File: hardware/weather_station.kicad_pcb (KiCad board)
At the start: 2 copper layers, 70 parts, among them J1 USB_MICRO, Q1 BD135, Q2 BD135, SW1 SWITCH_SPDT, U1 nRF51x22, U2 TMP112, U3 BMP280, U4 Si7013, U5 LM3668, U6 MCP73831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

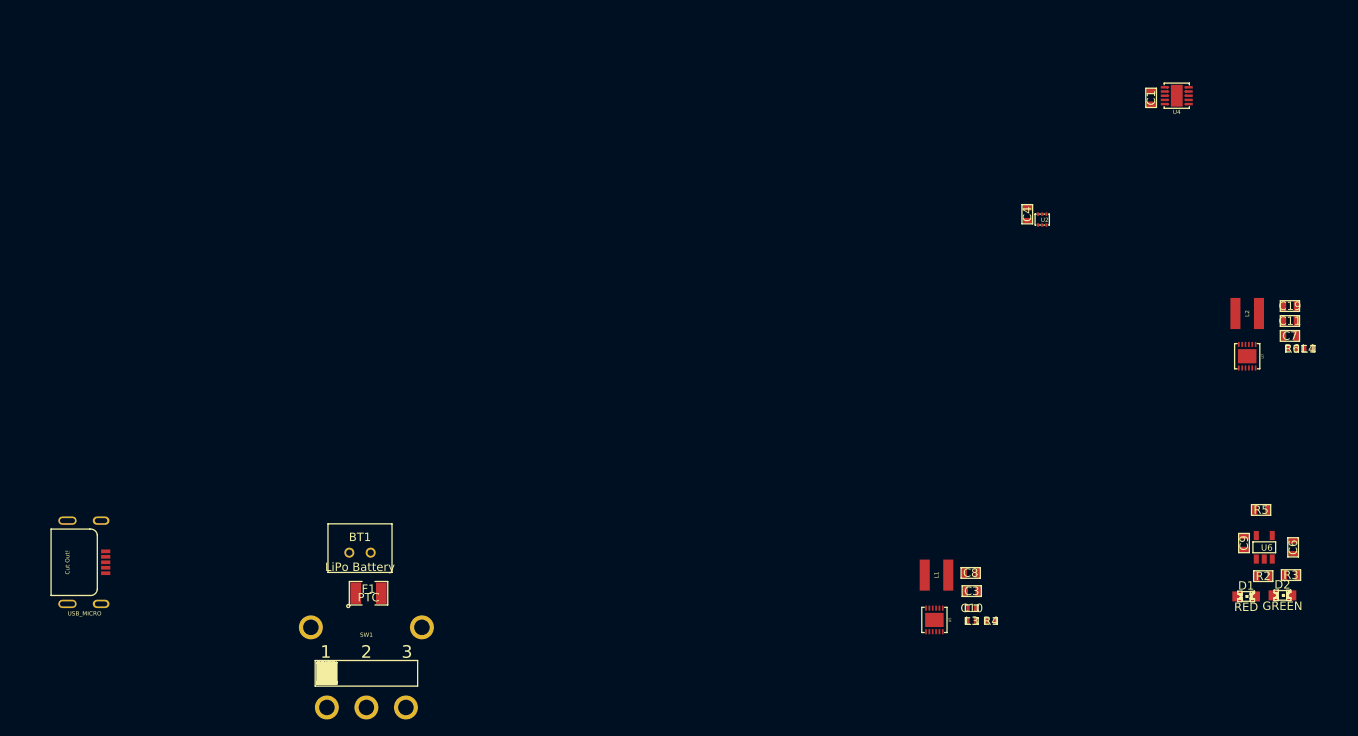
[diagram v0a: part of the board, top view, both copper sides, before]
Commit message: Update layout. Place some groups of components strategically
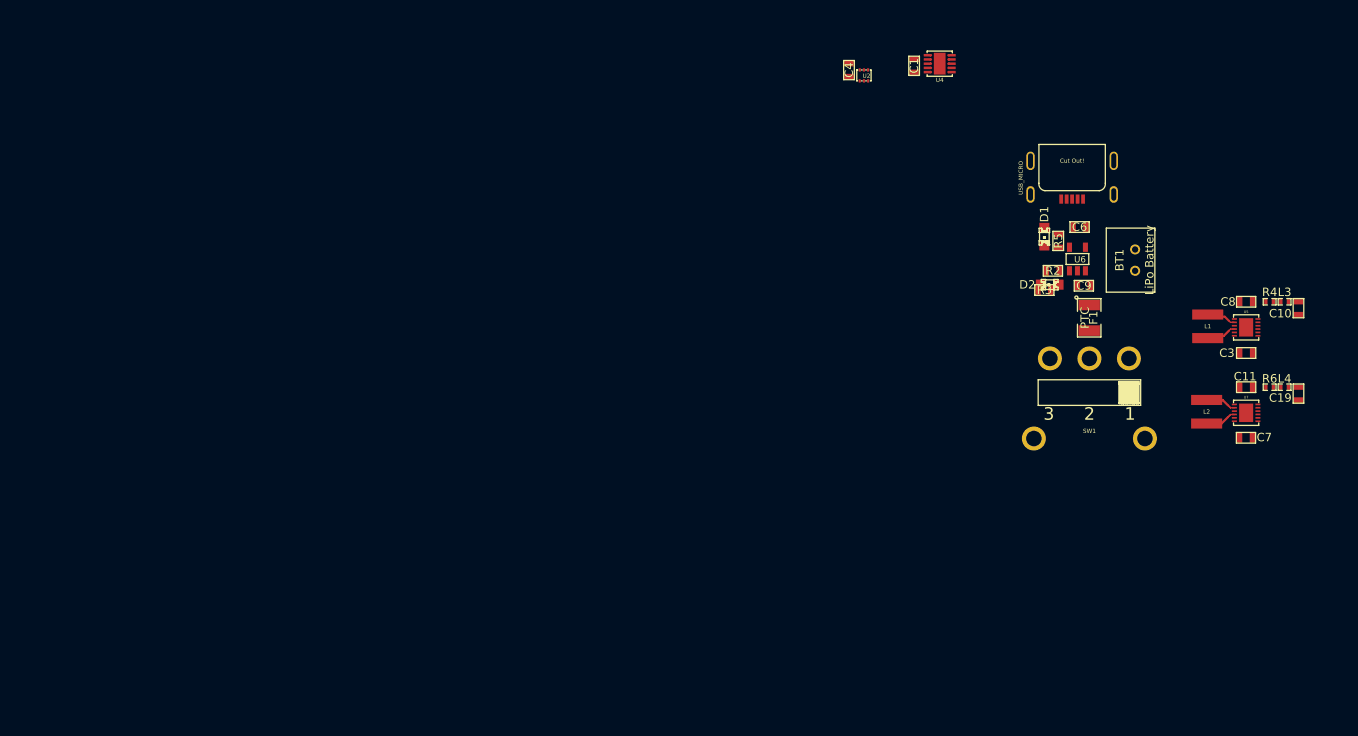
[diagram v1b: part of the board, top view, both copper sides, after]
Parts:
- C10: footprint SMD_Packages:SMD-0402 -> SMD_Packages:SMD-0603
- moved J1 128.7 mm to (234.4, 98.3), turned to 180 degrees
- moved BT1 98.6 mm to (241.9, 110.1), turned to 90 degrees
- moved SW1 95.5 mm to (236.5, 121.8), turned to 180 degrees
- moved F1 91.8 mm to (236.5, 117.0), turned to 270 degrees
- moved L3 53.2 mm to (259.7, 115.1)
- moved C10 52.8 mm to (261.4, 115.8), turned to 270 degrees
- moved U5 50.9 mm to (255.1, 118.1), turned to 90 degrees
- moved R4 50.4 mm to (257.9, 115.1), turned to 180 degrees
- moved D1 49.1 mm to (231.1, 107.3), turned to 270 degrees
- moved D2 46.2 mm to (231.8, 113.0), turned to 180 degrees
- moved C8 46.0 mm to (255.1, 115.1), turned to 180 degrees
- moved C6 45.8 mm to (235.3, 106.2), turned to 180 degrees
- moved R3 44.8 mm to (231.1, 113.7), turned to 180 degrees
- moved R2 44.1 mm to (232.2, 111.4)
- moved L1 43.8 mm to (250.6, 118.0), turned to 270 degrees
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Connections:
- U5 pad 11: GND -> Net-(C8-Pad1)
- U5 pad 12: VIN -> Net-(C8-Pad1)
- U5 pad 7: Net-(C8-Pad1) -> VIN
- U5 pad 8: Net-(C8-Pad1) -> GND
- U7 pad 11: GND -> Net-(C11-Pad1)
- U7 pad 12: VIN -> Net-(C11-Pad1)
- U7 pad 7: Net-(C11-Pad1) -> VIN
- U7 pad 8: Net-(C11-Pad1) -> GND
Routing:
- net Net-(L2-Pad1): track 0.00 -> 7.30 mm
- net Net-(L2-Pad2): track 0.00 -> 5.26 mm
- net Net-(L1-Pad2): track 0.00 -> 3.62 mm
- net Net-(L1-Pad1): track 0.00 -> 3.56 mm
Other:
- net class Default: clearance 0.254 -> 0.1524
- net class Default2 added: clearance 0.1524, trace_width 0.254, via_dia 0.889, via_drill 0.635
- net class Default3 added: clearance 0.254, trace_width 0.254, via_dia 0.889, via_drill 0.635
- rule trace_clearance: 0.254 -> 0.1524
- rule trace_min: 0.254 -> 0.1524
- rule via_min_drill: 0.508 -> 0.1778
- rule via_min_size: 0.889 -> 0.3302

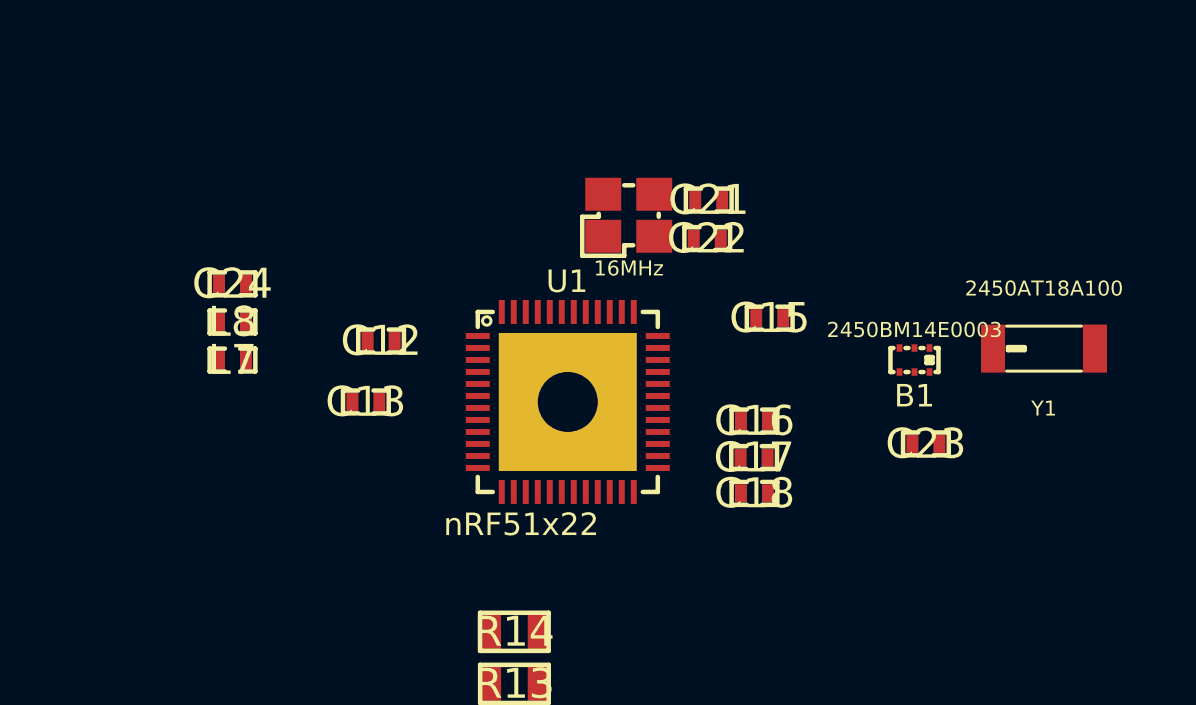
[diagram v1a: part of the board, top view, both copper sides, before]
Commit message: Place components around nRF51 device
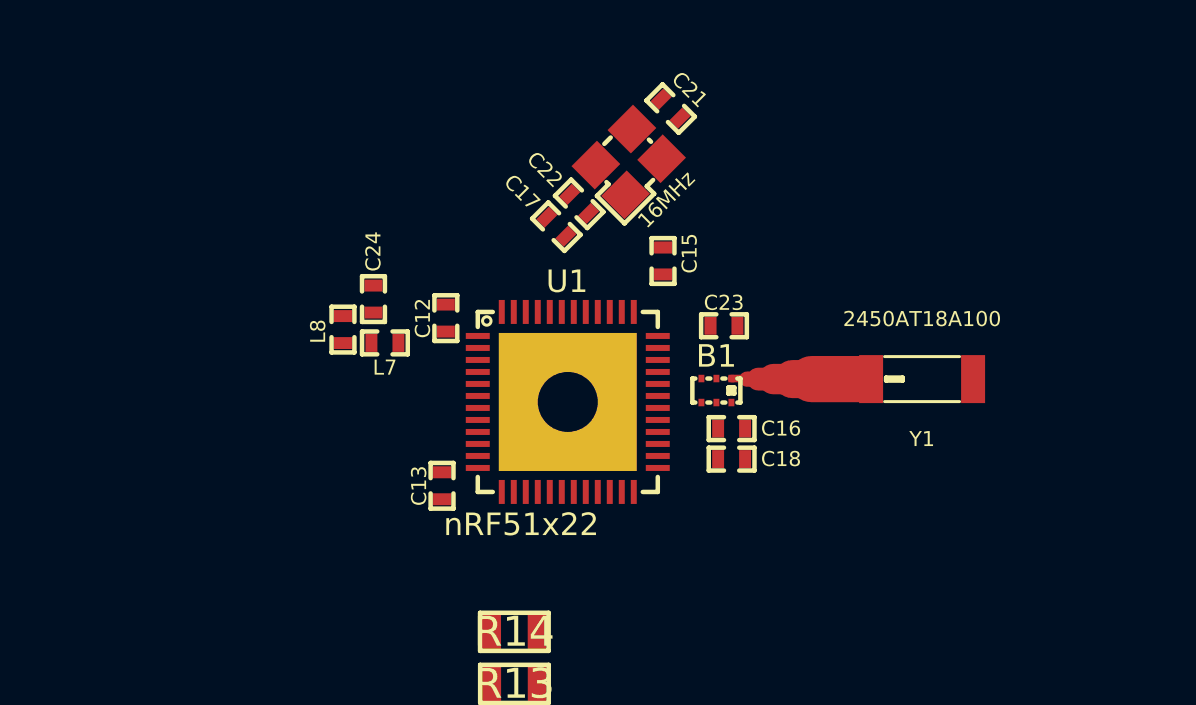
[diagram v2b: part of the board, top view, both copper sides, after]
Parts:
- moved C17 10.1 mm to (247.1, 35.7), turned to 135 degrees
- moved C23 7.80 mm to (252.7, 39.0)
- moved B1 6.68 mm to (252.5, 41.1)
- moved L7 5.11 mm to (241.4, 39.6), turned to 180 degrees
- moved C24 4.73 mm to (241.0, 38.1), turned to 90 degrees
- moved C22 4.42 mm to (247.9, 34.9), turned to 315 degrees
- moved Y1 4.19 mm to (259.3, 40.8)
- moved C15 4.03 mm to (250.7, 36.8), turned to 90 degrees
- moved C13 3.78 mm to (243.3, 44.3), turned to 270 degrees
- moved L8 3.69 mm to (240.0, 39.1), turned to 90 degrees
- moved C21 3.30 mm to (251.0, 31.8), turned to 315 degrees
- moved C12 2.29 mm to (243.5, 38.7), turned to 90 degrees
- moved X1 1.78 mm to (249.6, 33.5), turned to 45 degrees
- moved C18 1.37 mm to (253.0, 43.4)
- moved C16 0.80 mm to (253.0, 42.4), turned to 180 degrees
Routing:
- net Net-(B1-Pad1): track 0.00 -> 4.41 mm

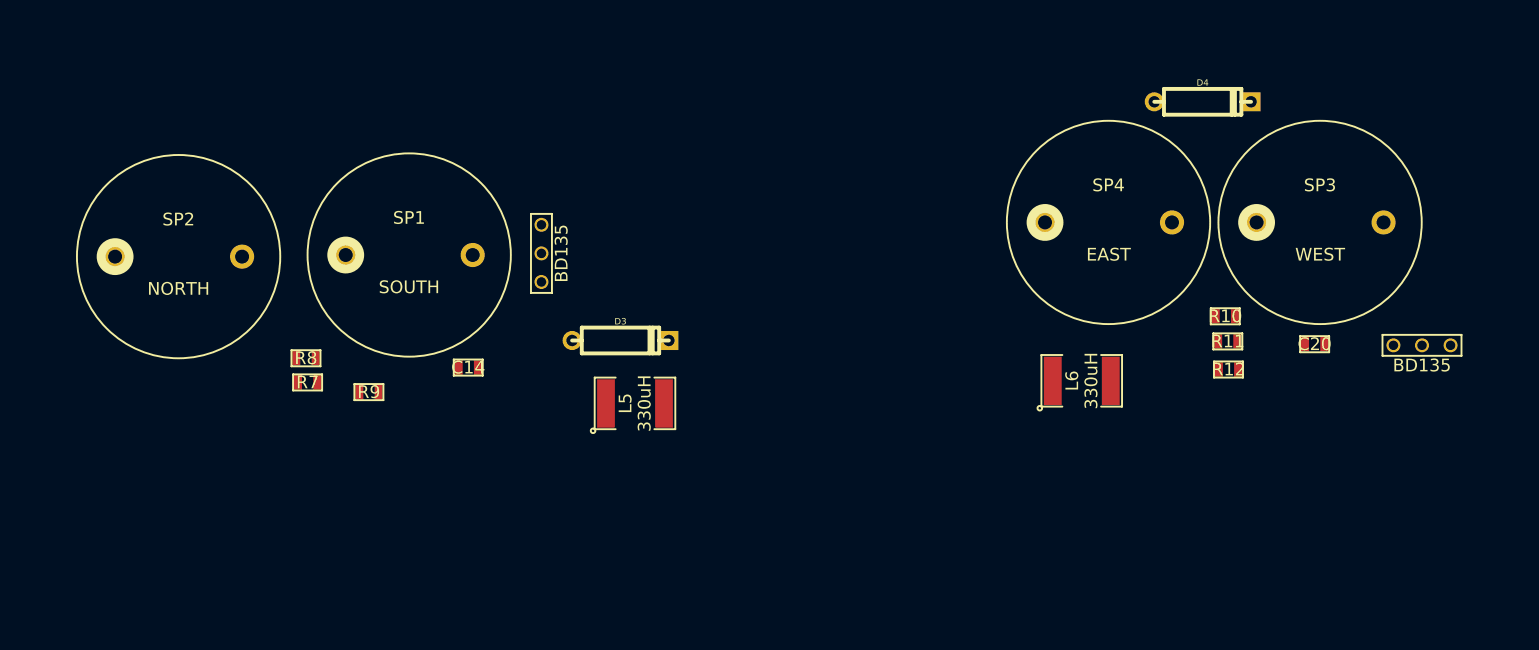
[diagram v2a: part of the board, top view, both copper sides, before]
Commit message: Group ultrasonic related components together
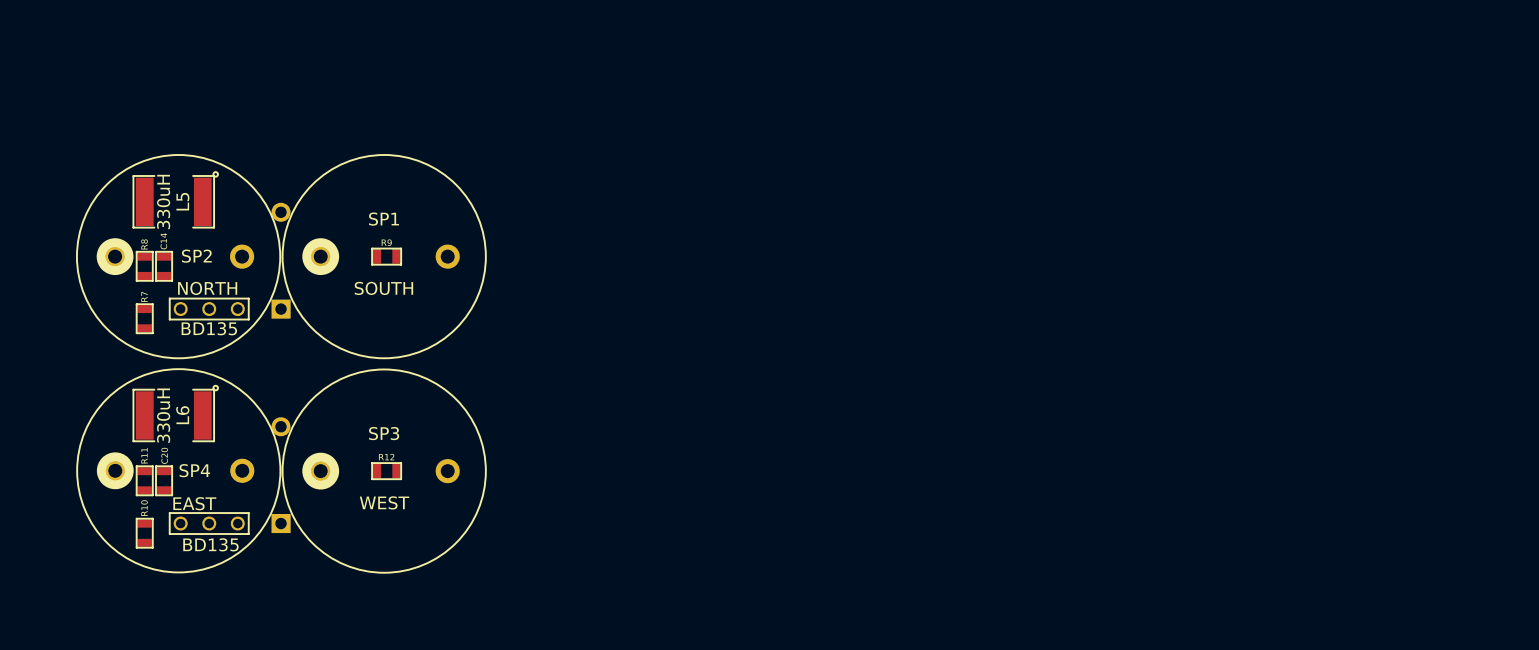
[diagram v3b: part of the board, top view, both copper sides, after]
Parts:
- D3, D4: moved to B.Cu
- moved Q2 96.5 mm to (95.0, 82.9), turned to 180 degrees
- moved C20 91.2 mm to (91.4, 79.5), turned to 270 degrees
- moved R10 86.8 mm to (89.9, 83.6), turned to 270 degrees
- moved R11 86.0 mm to (89.9, 79.5), turned to 270 degrees
- moved D4 78.3 mm to (100.6, 79.1), turned to 270 degrees
- moved SP3 76.3 mm to (108.8, 78.7)
- moved SP4 75.8 mm to (92.6, 78.7)
- moved L6 71.6 mm to (92.2, 74.4), turned to 180 degrees
- moved R12 66.8 mm to (109.0, 78.7)
- moved L5 39.6 mm to (92.2, 57.5), turned to 180 degrees
- moved D3 27.5 mm to (100.6, 62.2), turned to 270 degrees
- moved Q1 26.5 mm to (95.0, 66.0), turned to 180 degrees
- moved C14 25.2 mm to (91.4, 62.6), turned to 270 degrees
- moved R8 14.6 mm to (89.9, 62.6), turned to 270 degrees
- moved R7 13.8 mm to (89.9, 66.7), turned to 270 degrees
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
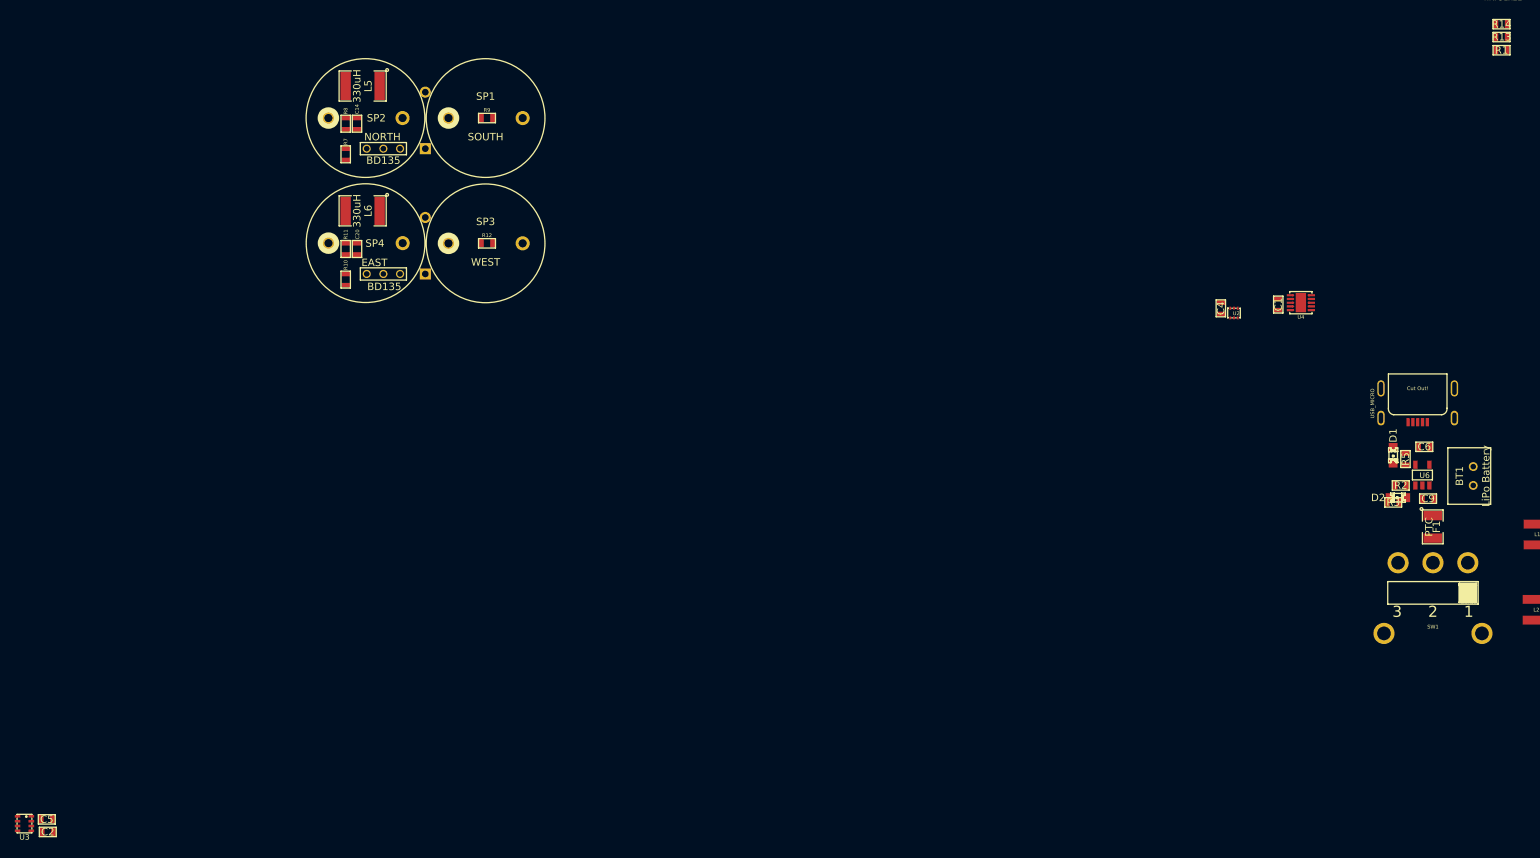
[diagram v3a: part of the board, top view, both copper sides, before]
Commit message: Group together I2C components and related components
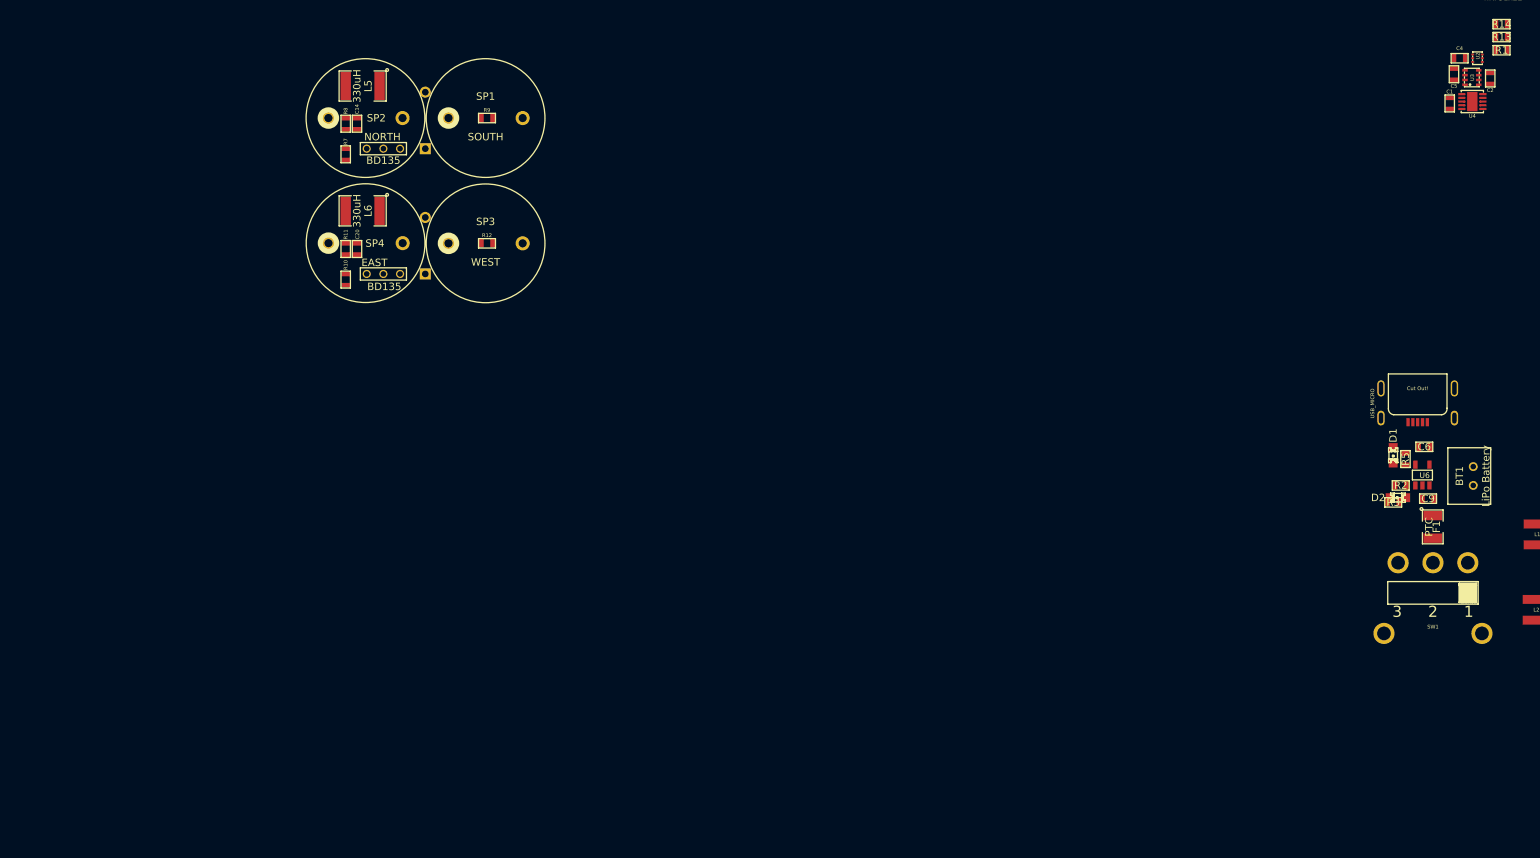
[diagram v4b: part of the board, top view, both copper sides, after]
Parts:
- moved U3 219.5 mm to (241.7, 56.4), turned to 180 degrees
- moved C2 219.4 mm to (244.2, 56.5), turned to 90 degrees
- moved C5 214.7 mm to (239.3, 55.9), turned to 270 degrees
- moved U2 47.5 mm to (242.5, 53.8), turned to 90 degrees
- moved C4 46.6 mm to (240.1, 53.8), turned to 180 degrees
- moved C1 35.6 mm to (238.8, 59.9)
- moved U4 35.6 mm to (241.8, 59.6)
